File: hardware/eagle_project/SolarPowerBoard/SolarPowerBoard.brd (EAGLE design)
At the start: 68.8 x 53.6 mm, 83 parts, among them J2 105017-0001_105017-0001, J3 BAT_ID, J5 XG8S-0331_XG8S-0331, K1 G6E-134P-US_DC5_G6E-134P-US_D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, Q1 SOLARCOMPONENTS_CSD16406Q3, Q2 SOLARCOMPONENTS_CSD16406Q3, Q3 DAVIDE_FDN302P, U1 SOLARCOMPONENTS_SVP1040, U2 SOLARCOMPONENTS_MAX17260, U3 FT230XQ_FT230XQ_2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

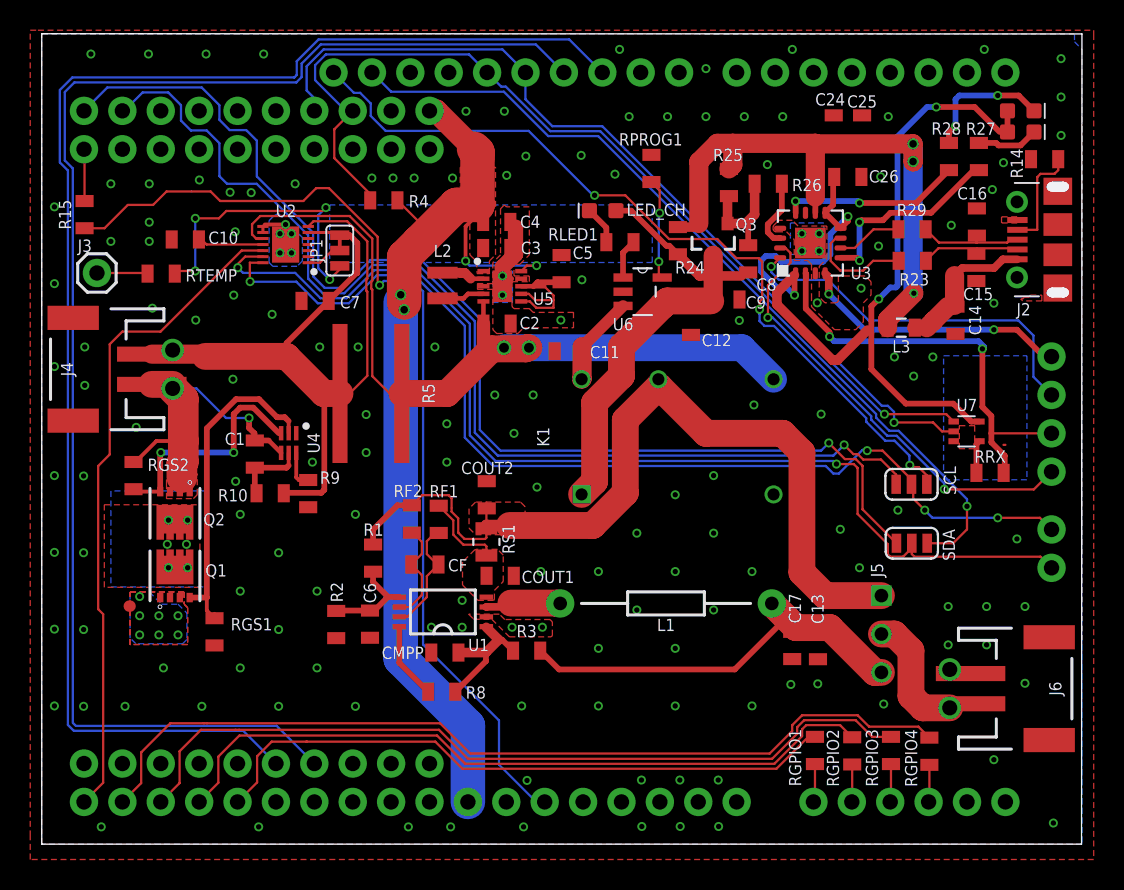
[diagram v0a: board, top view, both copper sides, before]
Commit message: Hardware: reset out pin now can be routed to DIO22 instead of DIO1 which is reserved for the rf switch on cc1350 launchpads
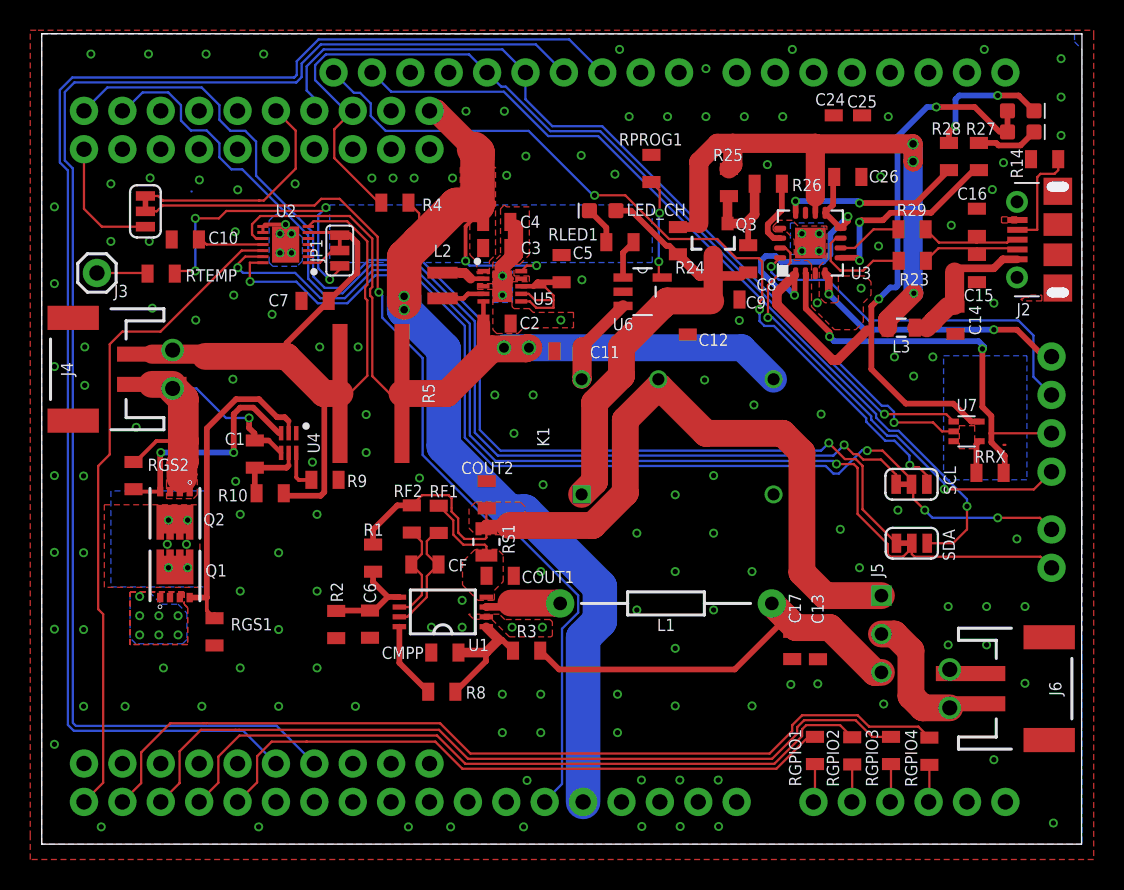
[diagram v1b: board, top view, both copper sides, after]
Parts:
- removed R15: 0, SolarPowerBoard:SPARKFUN-RESISTORS_0805
- added RES_SEL: POWERSOL_JUMPER-SMT_3_0_SILK, SolarPowerBoard:POWERSOL_SMT-JUMPER_3_0_NC_TRACE_SILK
- RGPIO1, RGPIO2, RGPIO3, RGPIO4: value 1k -> DNM
- moved R9 1.44 mm to (18.0, 23.6), turned to 0 degrees
- moved R4 0.75 mm to (22.6, 41.9)
- moved C12 0.21 mm to (42.0, 34.1)
- moved C15 0.08 mm to (61.1, 37.6)
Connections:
- removed net DIO1-RESET: B1.DIO1-RESET, R15.2
- removed net N$40: B2.DIO1-RESET, R15.1
- new net DIO1_RESERVED: B1.DIO1-RESET, RES_SEL.3
- new net DIO22: B1.DIO22, RES_SEL.1
- new net NRF_RESET: B2.DIO1-RESET, RES_SEL.2
- net VDD: now also B2.VDD@2; no longer B2.VDD
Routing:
- net N$40: track 66.3 -> 0.00 mm, vias 1 -> 0
- net NRF_RESET: track 0.00 -> 61.2 mm, vias 0 -> 1
- net DIO22: track 0.00 -> 15.3 mm
- net DIO1_RESERVED: track 0.00 -> 8.49 mm
- net VDD: track 65.3 -> 69.8 mm
- net DIO1-RESET: track 3.44 -> 0.00 mm
- net N$37: track 72.9 -> 72.1 mm
- net PO.25(RX)-DIO3(TX): track 65.1 -> 65.6 mm
- net GND: track 7.20 -> 7.15 mm, vias 165 -> 164
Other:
- board text added: "ALRT"
- board text added: "DIO1"
- board text added: "DIO22"
- board text added: "GND"
- board text added: "IO1"
- board text added: "IO2"
- board text added: "IO3"
- board text added: "IO4"
- board text added: "VDD"
- board text added: "nRF_RST"
